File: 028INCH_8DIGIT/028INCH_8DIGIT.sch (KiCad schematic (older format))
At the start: 11 parts, among them J1 Conn_01x04_Female, J2 Conn_01x04_Male, U1 JM-S03651BH, U2 TM1637, U3 CC56-12CGKWA

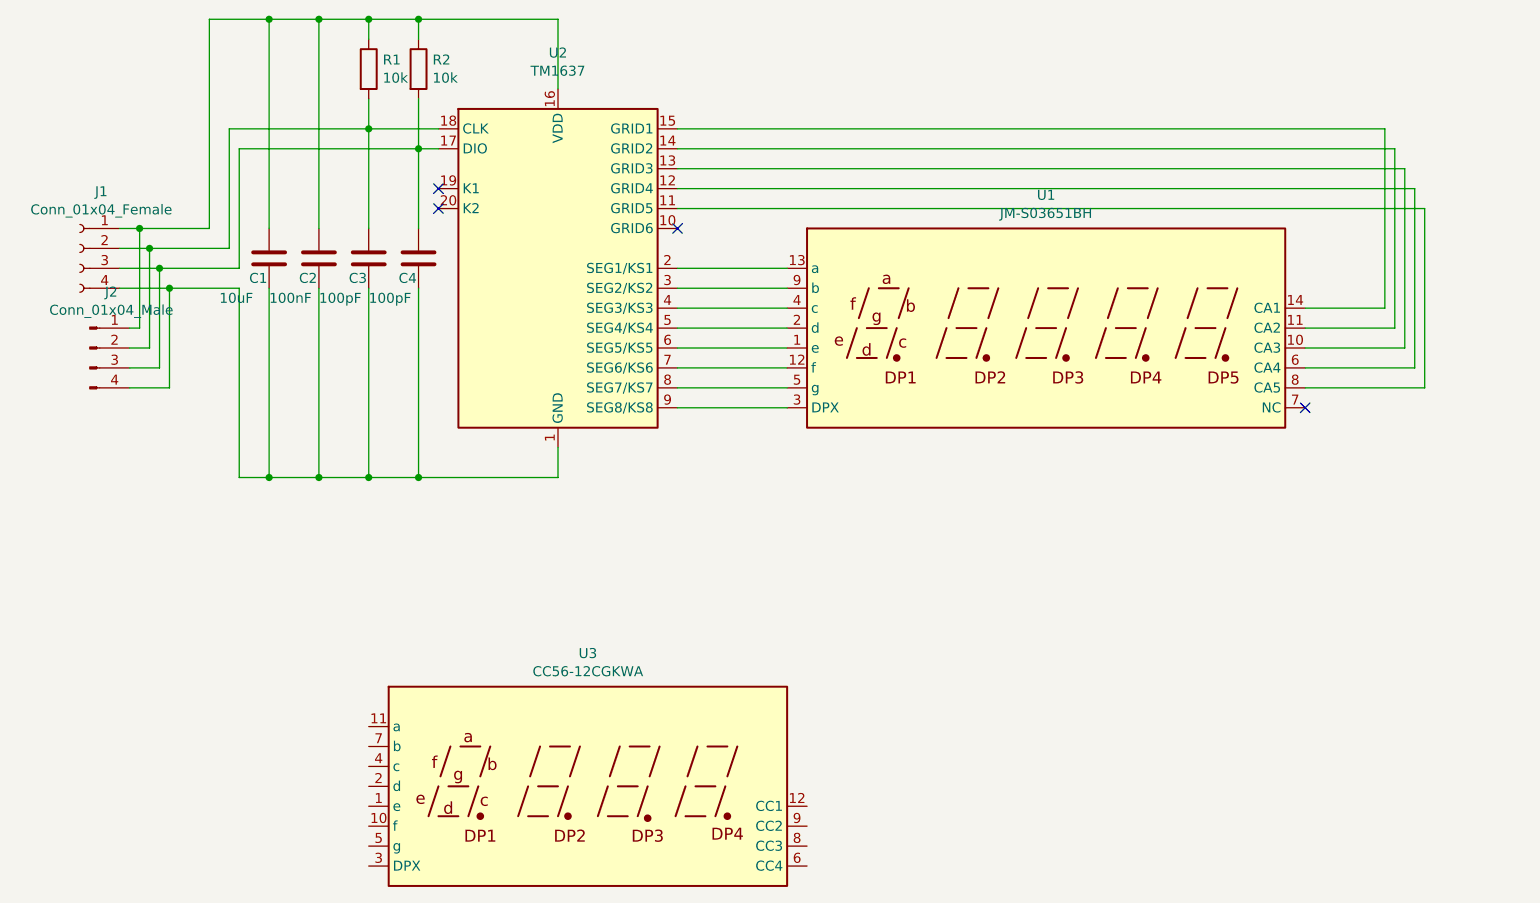
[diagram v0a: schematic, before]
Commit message: start element placing
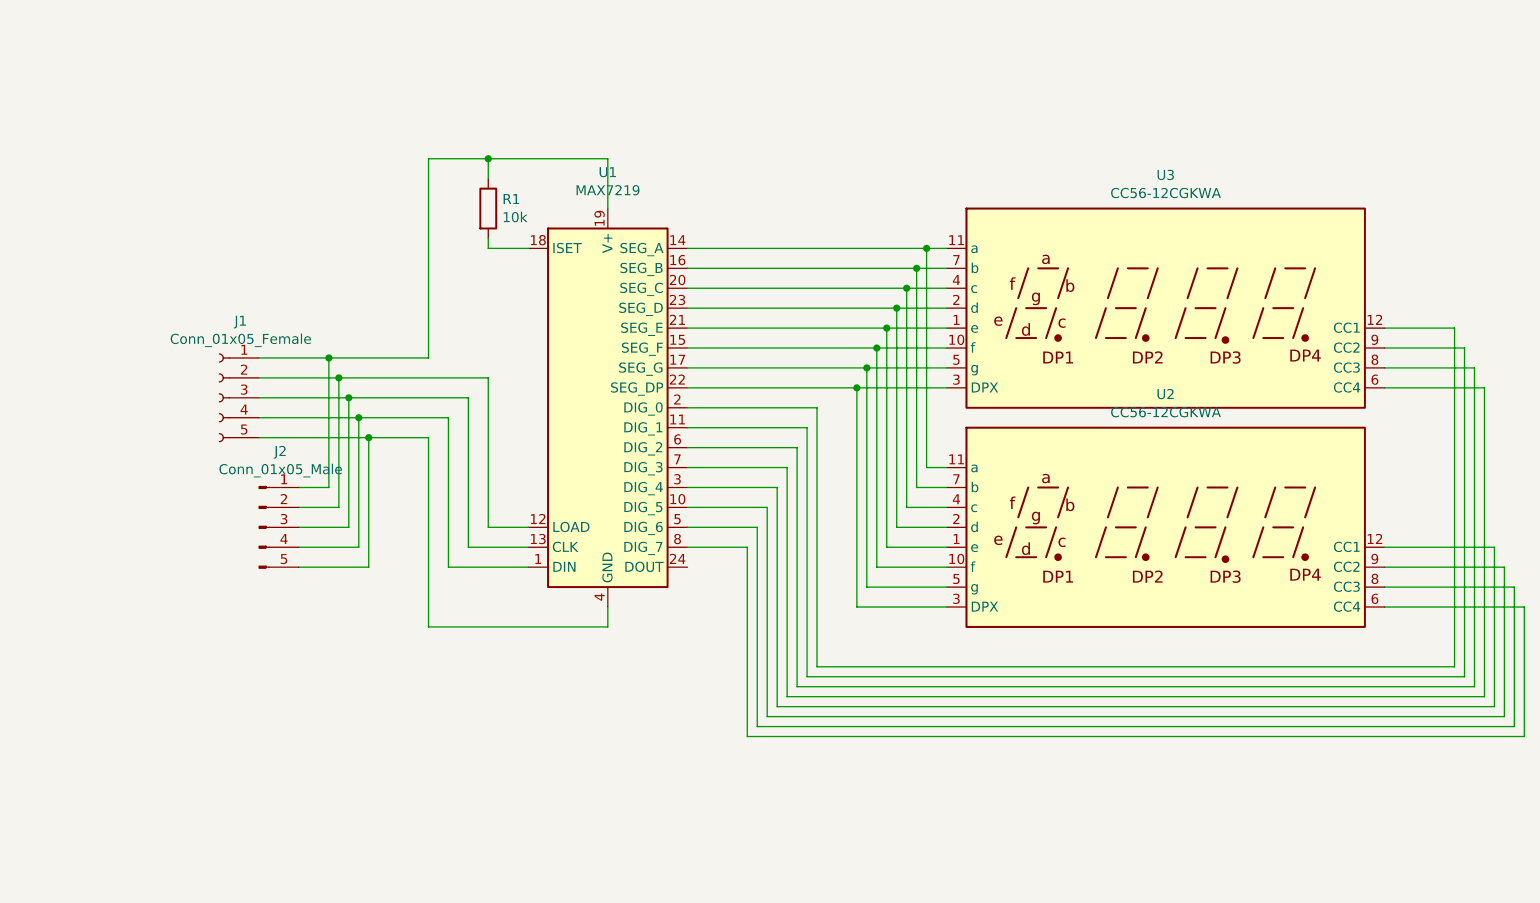
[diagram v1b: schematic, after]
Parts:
- removed C1: 10uF, Capacitor_SMD:C_0805_2012Metric_Pad1.15x1.40mm_HandSolder, symbol Device:C
- removed C2: 100nF, Capacitor_SMD:C_0805_2012Metric_Pad1.15x1.40mm_HandSolder, symbol Device:C
- removed C3, C4: 100pF, Capacitor_SMD:C_0805_2012Metric_Pad1.15x1.40mm_HandSolder, symbol Device:C
- removed J1: Conn_01x04_Female, TerminalBlock_4Ucon:TerminalBlock_4Ucon_1x04_P3.50mm_Horizontal, symbol Connector:Conn_01x04_Female
- removed J2: Conn_01x04_Male, Connector_PinHeader_2.54mm:PinHeader_1x04_P2.54mm_Vertical, symbol Connector:Conn_01x04_Male
- removed R2: 10k, Resistor_SMD:R_0805_2012Metric_Pad1.15x1.40mm_HandSolder, symbol Device:R
- removed U1: JM-S03651BH, JINGMEI:JM-S03651BH, symbol jingmei:JM-S03651BH
- removed U2: TM1637, Package_SO:SO-20_12.8x7.5mm_P1.27mm, symbol titanmicroelectronics:TM1637
- added J1: Conn_01x05_Female, TerminalBlock_4Ucon:TerminalBlock_4Ucon_1x05_P3.50mm_Horizontal, symbol Connector:Conn_01x05_Female
- added J2: Conn_01x05_Male, Connector_PinHeader_2.54mm:PinHeader_1x05_P2.54mm_Vertical, symbol Connector:Conn_01x05_Male
- added U1: MAX7219, Package_SO:SOIC-24W_7.5x15.4mm_P1.27mm, symbol Driver_LED:MAX7219
- added U2: CC56-12CGKWA, XLITX:2841AS, symbol Display_Character:CC56-12CGKWA
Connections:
- net at R1.1: now also J1.1 (Pin_1), J2.1 (Pin_1), U1.19 (V+)
- net at R1.2: now also U1.18 (ISET)
- net at U3.1 (e): now also U1.21 (SEG_E), U2.1 (e)
- net at U3.10 (f): now also U1.15 (SEG_F), U2.10 (f)
- net at U3.11 (a): now also U1.14 (SEG_A), U2.11 (a)
- net at U3.12 (CC1): now also U1.2 (DIG_0)
- net at U3.2 (d): now also U1.23 (SEG_D), U2.2 (d)
- net at U3.3 (DPX): now also U1.22 (SEG_DP), U2.3 (DPX)
- net at U3.4 (c): now also U1.20 (SEG_C), U2.4 (c)
- net at U3.5 (g): now also U1.17 (SEG_G), U2.5 (g)
- net at U3.6 (CC4): now also U1.7 (DIG_3)
- net at U3.7 (b): now also U1.16 (SEG_B), U2.7 (b)
- net at U3.8 (CC3): now also U1.6 (DIG_2)
- net at U3.9 (CC2): now also U1.11 (DIG_1)
- new net: J1.4 (Pin_4), J2.4 (Pin_4), U1.1 (DIN)
- new net: U1.10 (DIG_5), U2.9 (CC2)
- new net: J1.2 (Pin_2), J2.2 (Pin_2), U1.12 (LOAD)
- new net: J1.3 (Pin_3), J2.3 (Pin_3), U1.13 (CLK)
- new net: U1.3 (DIG_4), U2.12 (CC1)
- new net: J1.5 (Pin_5), J2.5 (Pin_5), U1.4 (GND), U1.9 (GND)
- new net: U1.5 (DIG_6), U2.8 (CC3)
- new net: U1.8 (DIG_7), U2.6 (CC4)
- no-connect marks 4 -> 0
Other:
- moved on the sheet: U3

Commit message: all traces routed
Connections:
- no-connect marks 0 -> 1
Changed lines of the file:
@@
 Wire Wire Line
 	2050 4550 2350 4550
+NoConn ~ 3650 5200
 $EndSCHEMATC
